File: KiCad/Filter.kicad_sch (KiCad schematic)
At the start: 0 parts

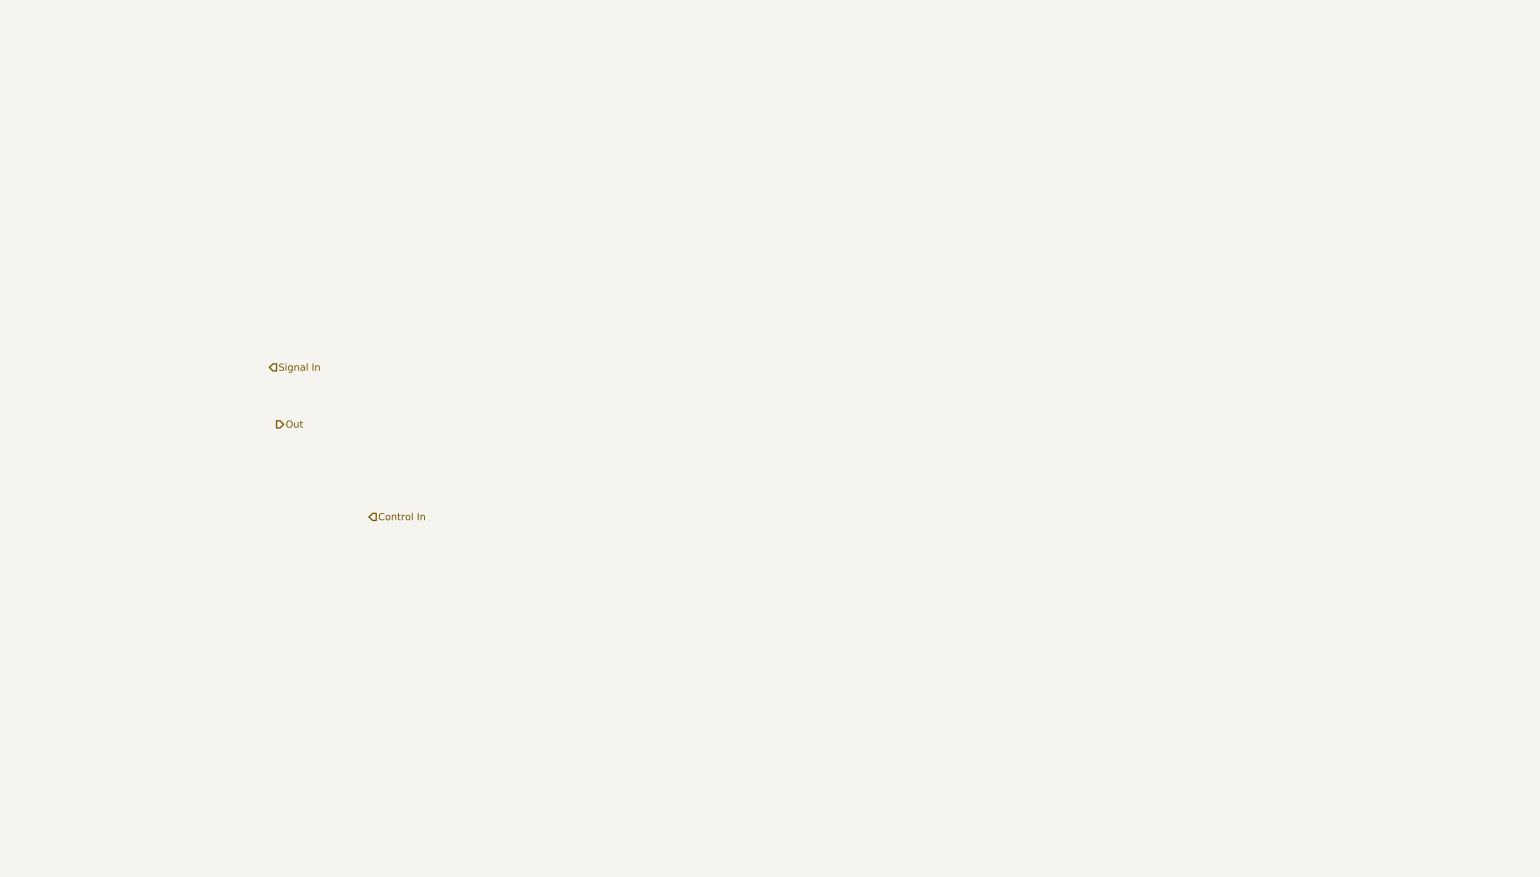
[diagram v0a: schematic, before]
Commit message: improved osc.'s output buffer cct., swap filter & amp
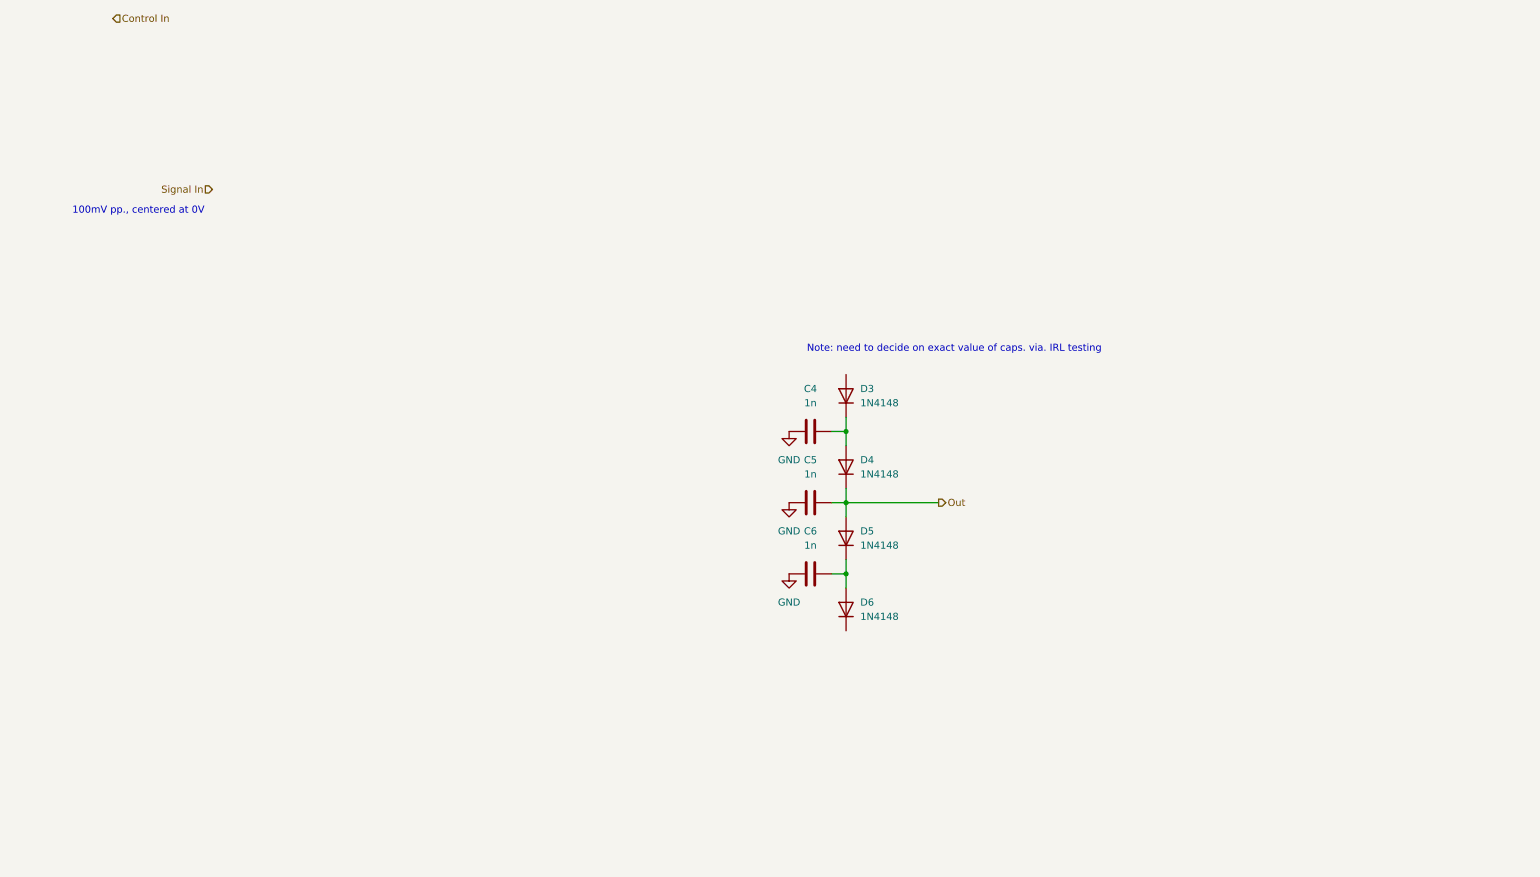
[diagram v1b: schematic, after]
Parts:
- added C4, C5, C6: 1n, symbol Device:C
- added D3, D4, D5, D6: 1N4148, Diode_THT:D_DO-35_SOD27_P7.62mm_Horizontal, symbol Diode:1N4148
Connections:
- net Out: now also C5.2, D4.1 (K), D5.2 (A)
- new net: C4.2, D3.1 (K), D4.2 (A)
- new net: C6.2, D5.1 (K), D6.2 (A)
- new net GND: C4.1, C5.1, C6.1
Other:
- note added: "100mV pp., centered at 0V"
- note added: "Note: need to decide on exact value of caps. via. IRL testing"

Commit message: made filter's core, but not CV and output ccts.
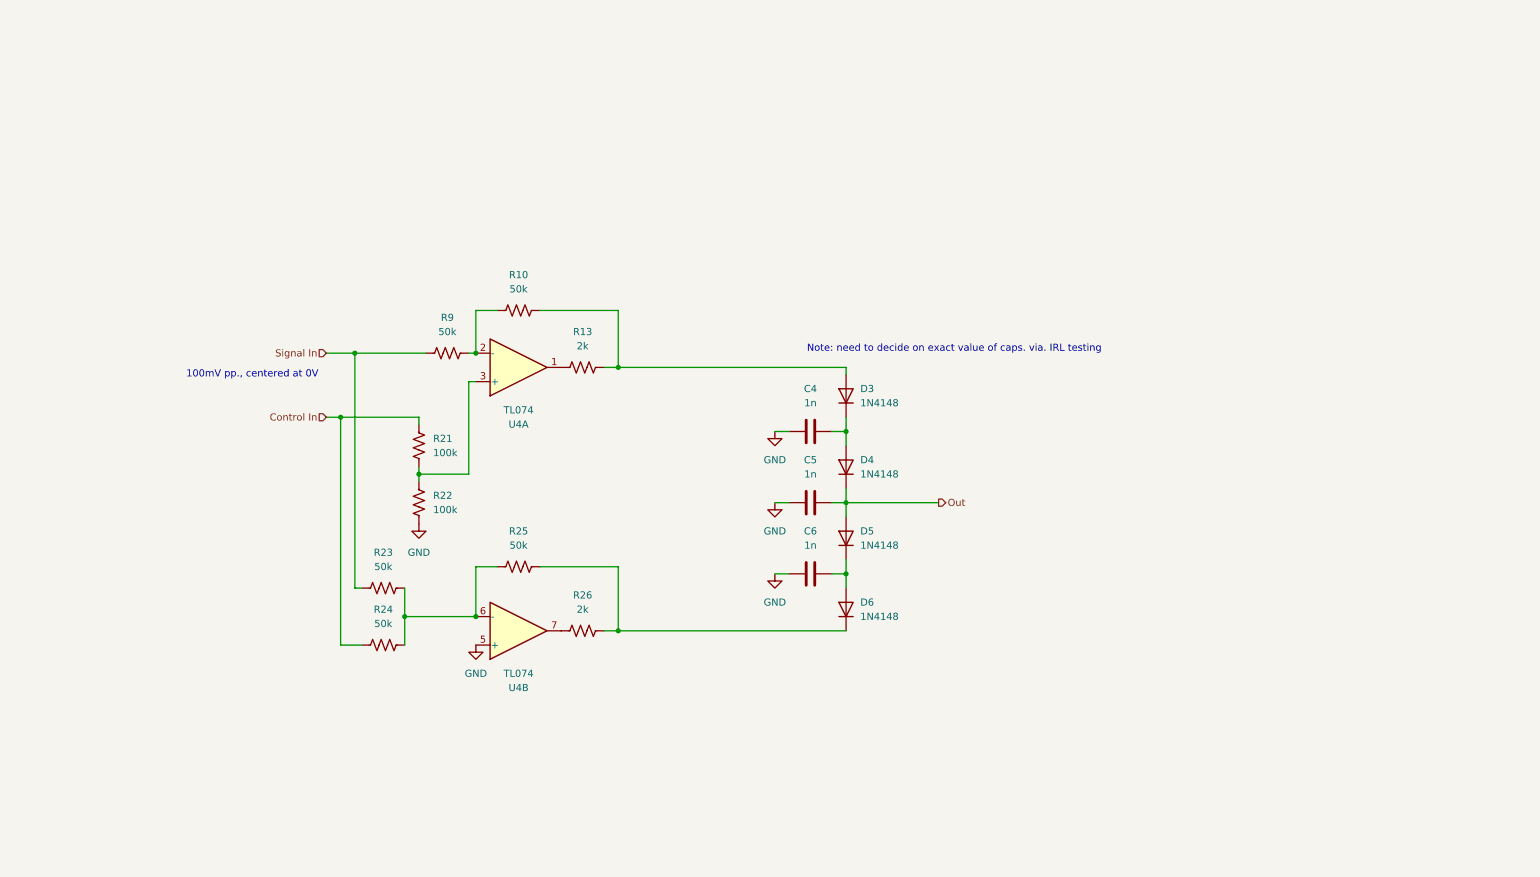
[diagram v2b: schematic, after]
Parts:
- added R10, R23, R24, R25, R9: 50k, symbol Device:R_US
- added R13, R26: 2k, symbol Device:R_US
- added R21, R22: 100k, symbol Device:R_US
- added U4: TL074, symbol Amplifier_Operational:TL074
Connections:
- net Control In: now also R21.2, R24.1
- net GND: now also R22.1, U4.5 (+)
- net Signal In: now also R23.1, R9.1
- net at D3.2 (A): now also R10.2, R13.1
- net at D6.1 (K): now also R25.2, R26.1
- new net: R10.1, R9.2, U4.2 (-)
- new net: R21.1, R22.2, U4.3 (+)
- new net: R23.2, R24.2, R25.1, U4.6 (-)
- new net: R26.2, U4.7
- new net: R13.2, U4.1

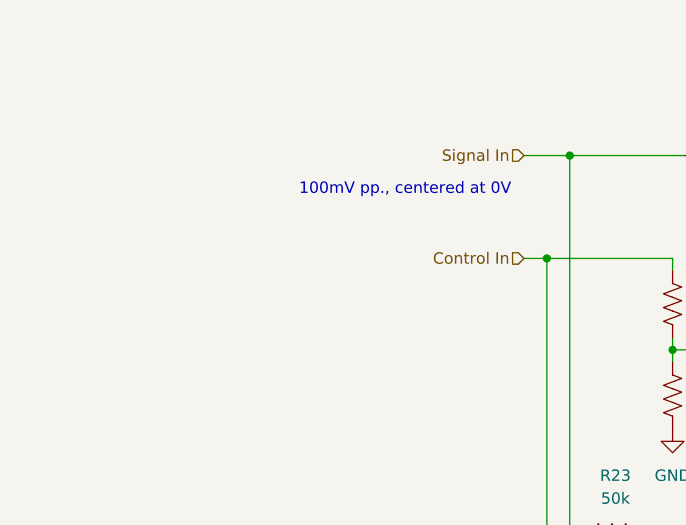
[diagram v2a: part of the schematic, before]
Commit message: added critical trimmer resistor that the osc. was missing
The trimmer resistor serves in a voltage divider to the osc.'s input signal. Without that voltage divider, the coarse tuning knob's range is too large (i.e. it's too coarse) and therefore unusable (according to the LTspice simualtions).
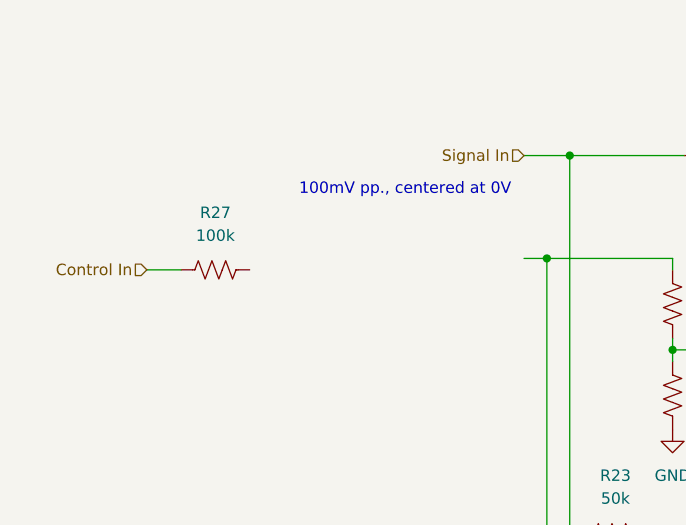
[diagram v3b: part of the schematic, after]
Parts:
- added R27: 100k, symbol Device:R_US
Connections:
- net Control In: now also R27.1; no longer R21.2, R24.1
- new net: R21.2, R24.1
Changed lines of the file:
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@@
+	(wire
+		(pts
+			(xy 22.86 90.17) (xy 26.67 90.17)
+		)
+		(stroke
+			(width 0)
+			(type default)
+		)
+	)
 	(wire
 		(pts
@@
 			(width 0)
 			(type default)
+		)
+	)
+	(hierarchical_label "Control In"
+		(shape input)
+		(at 22.86 90.17 180)
+		(effects
+			(font
+				(size 1.27 1.27)
+			)
+			(justify right)
 		)
 	)
@@
 		(shape input)
 		(at 64.77 77.47 180)
-		(effects
-			(font
-				(size 1.27 1.27)
-			)
-			(justify right)
-		)
-	)
-	(hierarchical_label "Control In"
-		(shape input)
-		(at 64.77 88.9 180)
 		(effects
 			(font
@@
 					(unit 1)
 				)
+			)
+		)
+	)
+	(symbol
+		(lib_id "Device:R_US")
+		(at 30.48 90.17 90)
+		(unit 1)
+		(body_style 1)
+		(exclude_from_sim no)
+		(in_bom yes)
+		(on_board yes)
+		(in_pos_files yes)
+		(dnp no)
+		(fields_autoplaced yes)
+		(property "Reference" "R27"
+			(at 30.48 83.82 90)
+			(show_name no)
+			(do_not_autoplace no)
+			(effects
+				(font
+					(size 1.27 1.27)
+				)
+			)
+		)
+		(property "Value" "100k"
+			(at 30.48 86.36 90)
+			(show_name no)
+			(do_not_autoplace no)
+			(effects
+				(font
+					(size 1.27 1.27)
+				)
+			)
+		)
+		(property "Footprint" ""
+			(at 30.734 89.154 90)
+			(hide yes)
+			(show_name no)
+			(do_not_autoplace no)
+			(effects
+				(font
+					(size 1.27 1.27)
+				)
+			)
+		)
+		(property "Datasheet" ""
+			(at 30.48 90.17 0)
+			(hide yes)
+			(show_name no)
+			(do_not_autoplace no)
+			(effects
+				(font
+					(size 1.27 1.27)
+				)
+			)
+		)
+		(property "Description" "Resistor, US symbol"
+			(at 30.48 90.17 0)
+			(hide yes)
+			(show_name no)
+			(do_not_autoplace no)
+			(effects
+				(font
+					(size 1.27 1.27)
+				)
+			)
+		)
+		(pin "1"
+		)
+		(pin "2"
+		)
+		(instances
+			(project "Electronic Trombone"
+				(path "/931827f3-33b7-460f-8885-7db258da2648/6d65ef8f-8235-46d4-95e7-69caf9b93e91"
+					(reference "R27")
+					(unit 1)
+				)

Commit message: drafted filter schematic
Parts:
- added C7: 1u, Capacitor_THT:C_Rect_L7.5mm_W6.5mm_P5.00mm, symbol Device:C
- added D5, D7, D8: 1N4148, Diode_THT:D_DO-35_SOD27_P7.62mm_Horizontal, symbol Diode:1N4148
- added R27: 100k, symbol Device:R_US
- added R29: 10k, symbol Device:R_US
- added R34, R35: R_US, symbol Device:R_US
- added R36: 100k, Resistor_SMD:R_0201_0603Metric, symbol Device:R_US
- added RV6: 100k, symbol Device:R_Potentiometer_US
- added unit 3 of U4
- added unit 4 of U4
- added U5: TL074, symbol Amplifier_Operational:TL074
- renumbered D5 to D6, D6 to D9, R10 to R22, R27 to R23, R9 to R24, R13 to R25, R21 to R26, R22 to R28, R25 to R30, R23 to R31, R26 to R32, R24 to R33
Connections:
- net GND: now also D8.1 (K), R29.1, R36.1, U5.3 (+)
- net Out: now also U5.6 (-), U5.7; no longer C5.2, D4.1 (K), D6.2 (A)
- net Processed Control: now reaches R26.2, R33.1
- net Processed Control: now also U4.8, U4.9 (-)
- net at R23.2: now also D5.2 (A), R27.2, R29.2, U4.10 (+)
- new net: D7.1 (K), D8.2 (A)
- new net: D5.1 (K), D7.2 (A)
- new net: R35.1, U4.13 (-), U4.14
- new net: R34.1, R35.2, U5.2 (-)
- new net: C7.1, R34.2, U5.1
- new net: R27.1, RV6.2
- new net: C7.2, R36.2, U5.5 (+)
- new net +9V: RV6.1
- new net -9V: RV6.3
- new net Unprocessed Out: C5.2, D4.1 (K), D6.2 (A), U4.12 (+)
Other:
- note added: "10mV pp., centered at 0V"
- note added: "Find exact value -> thru. experimenting"
- note added: "Find exact values of caps. thru. experimenting ->"
- note added: "Find the resistances needed to amplify signal ->"
- note added: "Sets the control to a range tolerable to the diode ladder"
- note added: "Signal In with neg. offset"
- note added: "Signal In with pos. offset"
- note removed: "Note: need to decide on exact value of caps. via. IRL testing"
- moved on the sheet: C4, C5, C6, D3, D4, D6, D9, R22, R23, R24, R25, R26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

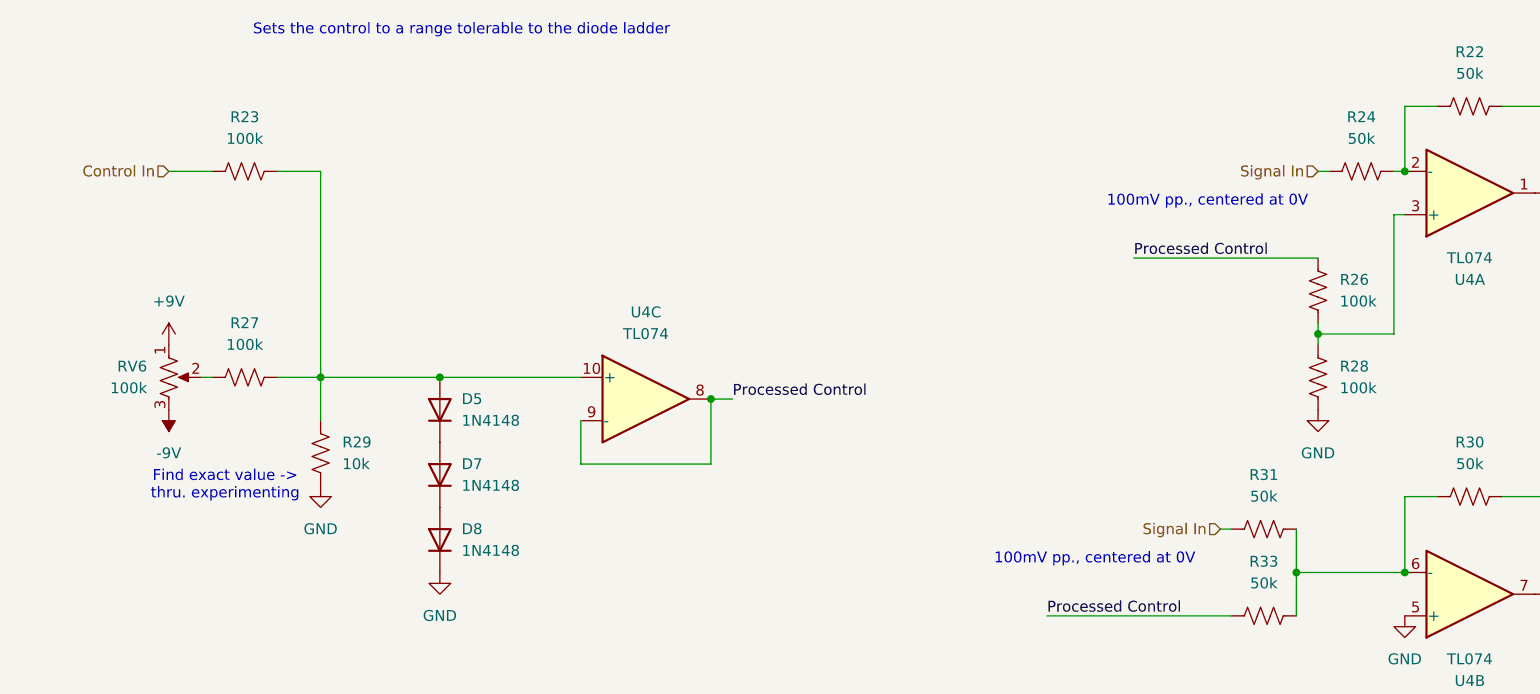
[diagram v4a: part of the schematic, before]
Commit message: created SPICE sim for Voltage Controlled Filter
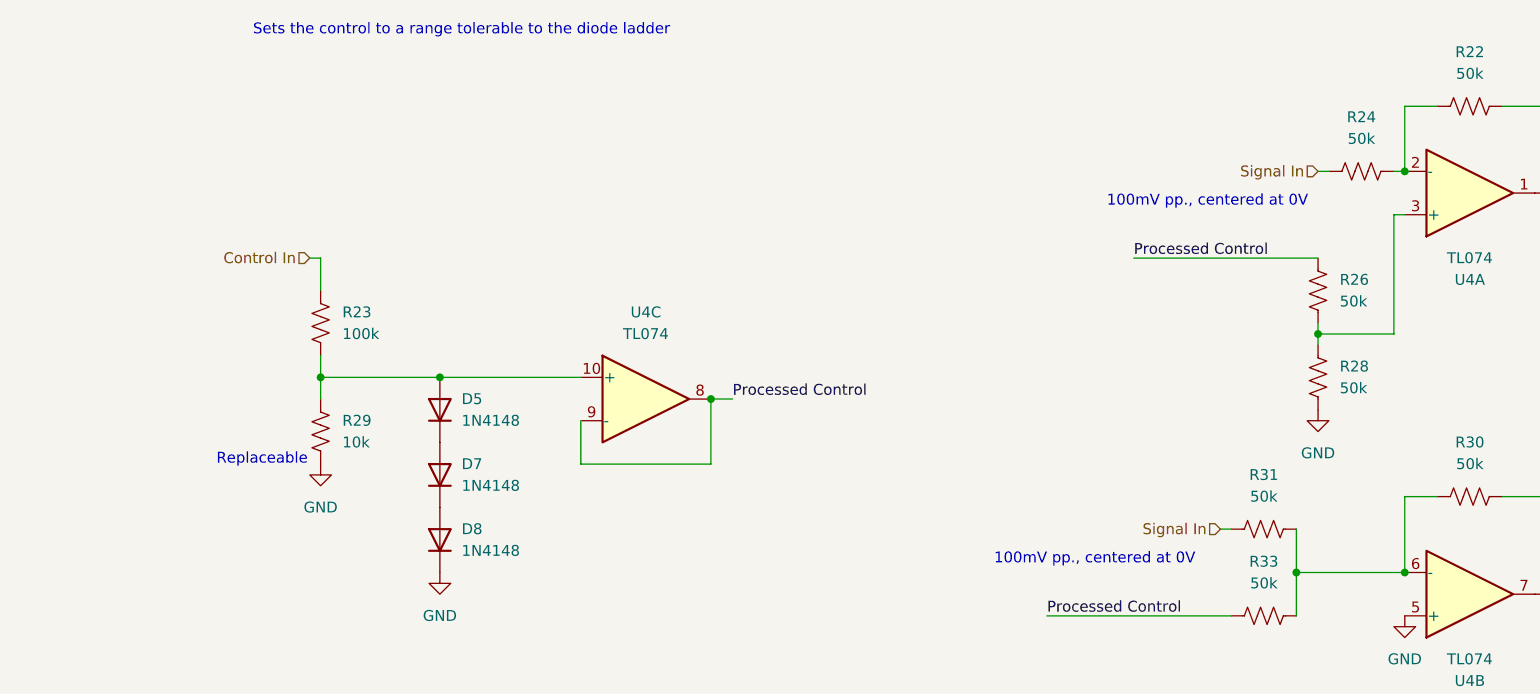
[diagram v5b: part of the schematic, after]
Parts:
- removed R27: 100k, symbol Device:R_US
- removed RV6: 100k, symbol Device:R_Potentiometer_US
- R26, R28: value 100k -> 50k
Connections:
- net Control In: now also R23.2; no longer R23.1
- net at D5.2 (A), R29.2, U4.10 (+): now also R23.1; no longer R23.2
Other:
- note added: "Replaceable"
- note removed: "Find exact value -> thru. experimenting"
- moved on the sheet: R23, R29

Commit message: finalizing schematic
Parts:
- removed C7: 1u, Capacitor_THT:C_Rect_L7.5mm_W6.5mm_P5.00mm, symbol Device:C
- removed R36: 100k, Resistor_SMD:R_0201_0603Metric, symbol Device:R_US
- R35: renamed from R25; value 2k -> 1k
- R37: renamed from R23; value 100k -> R_US
- R39: renamed from R29; value 10k -> R_US
- R42: renamed from R32; value 2k -> 1k
- renumbered C4 to C5, C5 to C6, C6 to C7, R22 to R33, R24 to R34, R26 to R36, R28 to R38, R30 to R40, R31 to R41, R33 to R43, R34 to R44, R35 to R45, U4 to U5, U5 to U6, U4 to U6
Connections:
- net GND: now also U5.10 (+), U6.5 (+); no longer U5.5 (+), U6.3 (+)
- net Out: now also U6.8, U6.9 (-); no longer U6.6 (-), U6.7
- net Processed Control: now also U5.1, U5.2 (-); no longer U5.8, U5.9 (-)
- net Unprocessed Out: now also U6.3 (+); no longer U6.12 (+)
- net at D5.2 (A), R37.1, R39.2: now also U5.3 (+); no longer U5.10 (+)
- net at R44.1, R45.2: now also U6.6 (-); no longer U6.2 (-)
- net at R44.2: now also U6.10 (+), U6.7; no longer U6.1
- net at R33.1, R34.2: now also U5.6 (-); no longer U5.2 (-)
- net at R36.1, R38.2: now also U5.5 (+); no longer U5.3 (+)
- net at R40.1, R41.2, R43.2: now also U5.9 (-); no longer U5.6 (-)
- net at R42.2: now also U5.8; no longer U5.7
- net at R35.2: now also U5.7; no longer U5.1
- new net: R45.1, U6.1, U6.2 (-)
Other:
- note removed: "Find the resistances needed to amplify signal ->"
- note removed: "Replaceable"
- moved on the sheet: U6C
